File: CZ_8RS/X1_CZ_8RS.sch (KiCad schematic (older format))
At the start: 68 parts, among them IC1 74LS541, IC10 74LS04, IC11 74LS20, IC12 8251, IC13 74LS08, IC14 74LS01, IC15 MAX232, IC16 74LS74, IC17 74LS32, IC18 MAX232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

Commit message: Add files via upload
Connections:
- net at IC17.4: now also IC16.5 (Q); no longer IC16.6 (~Q)
- no-connect marks 23 -> 22
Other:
- moved on the sheet: IC12, IC14A, IC14C, IC14D, IC16A, IC16B, IC17B, IC17D, IC2B, IC2D, IC4A, IC4B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

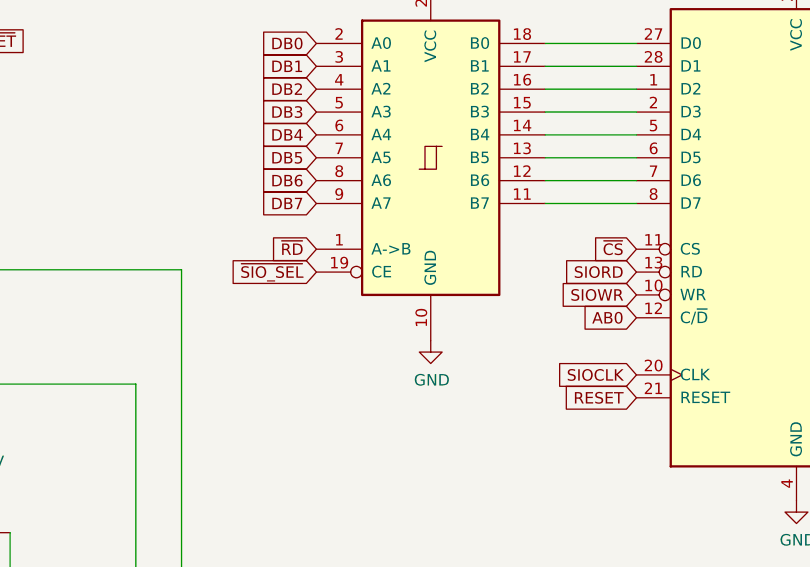
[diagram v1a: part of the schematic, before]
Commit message: corrected siosel, siord, and siowr line tag names
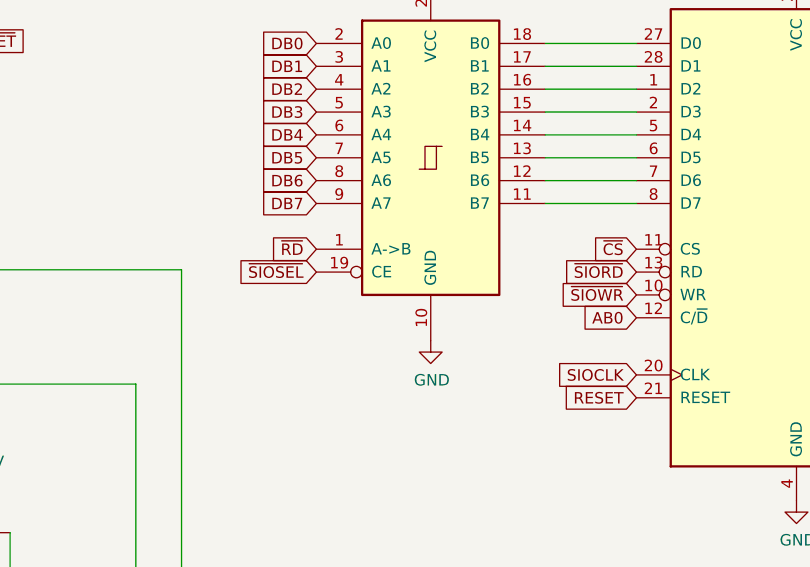
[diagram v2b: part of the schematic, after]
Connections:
- net SIORD is gone; now on net ~SIORD: IC12.13 (RD)
- net SIOWR is gone; now on net ~SIOWR: IC12.10 (WR)
- net ~SIO_SEL is gone; now on net ~SIOSEL: IC5.19 (CE)
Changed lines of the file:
@@
 ~RD
 Text GLabel 3840 5560 0    50   Input ~ 0
-~SIO_SEL
+~SIOSEL
 $Comp
 L power:+5V #PWR0134
@@
 ~CS
 Text GLabel 5240 5560 0    50   Input ~ 0
-SIORD
+~SIORD
 Text GLabel 5240 5660 0    50   Input ~ 0
-SIOWR
+~SIOWR
 Text GLabel 5240 5760 0    50   Input ~ 0
 AB0

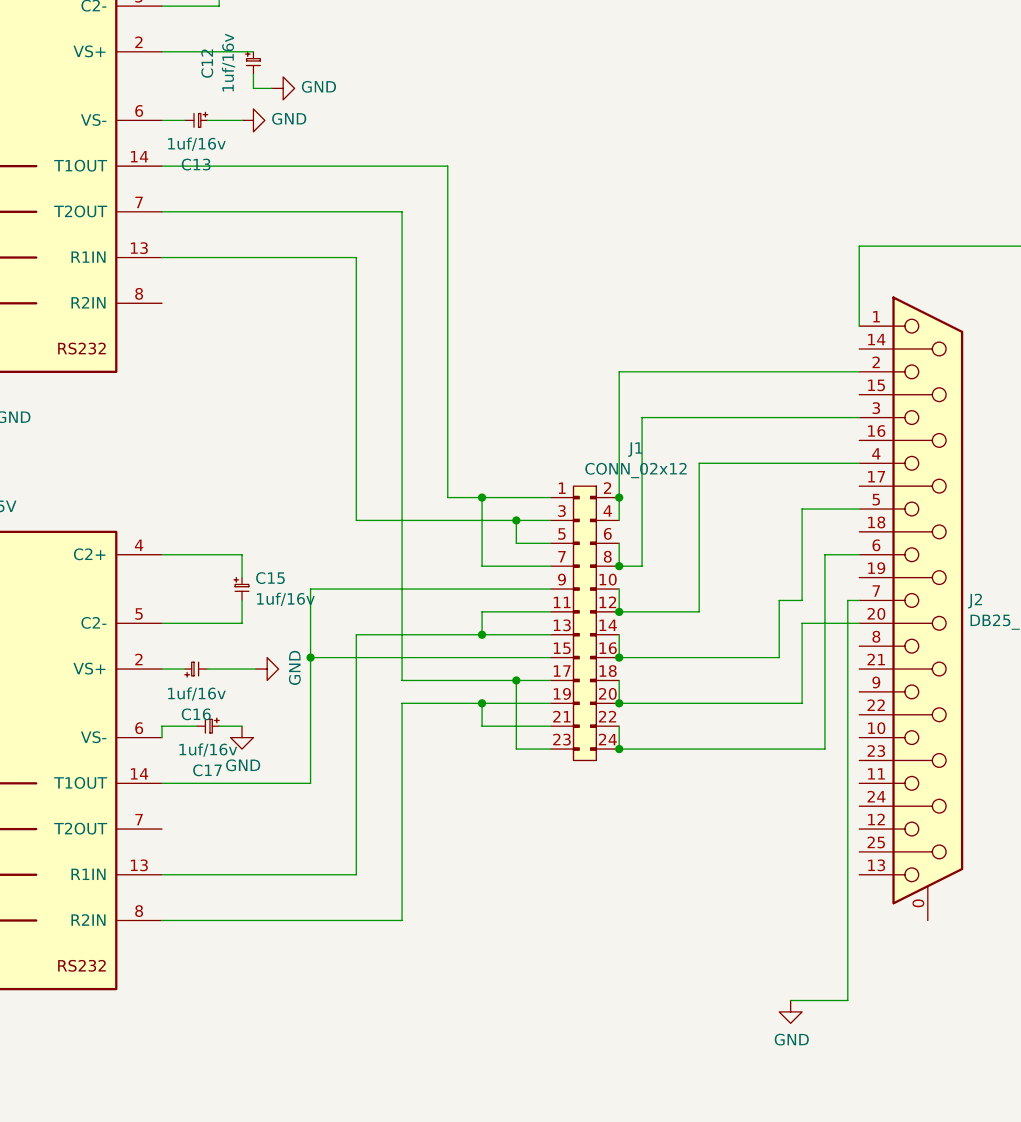
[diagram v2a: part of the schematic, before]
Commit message: added component names and jumper values
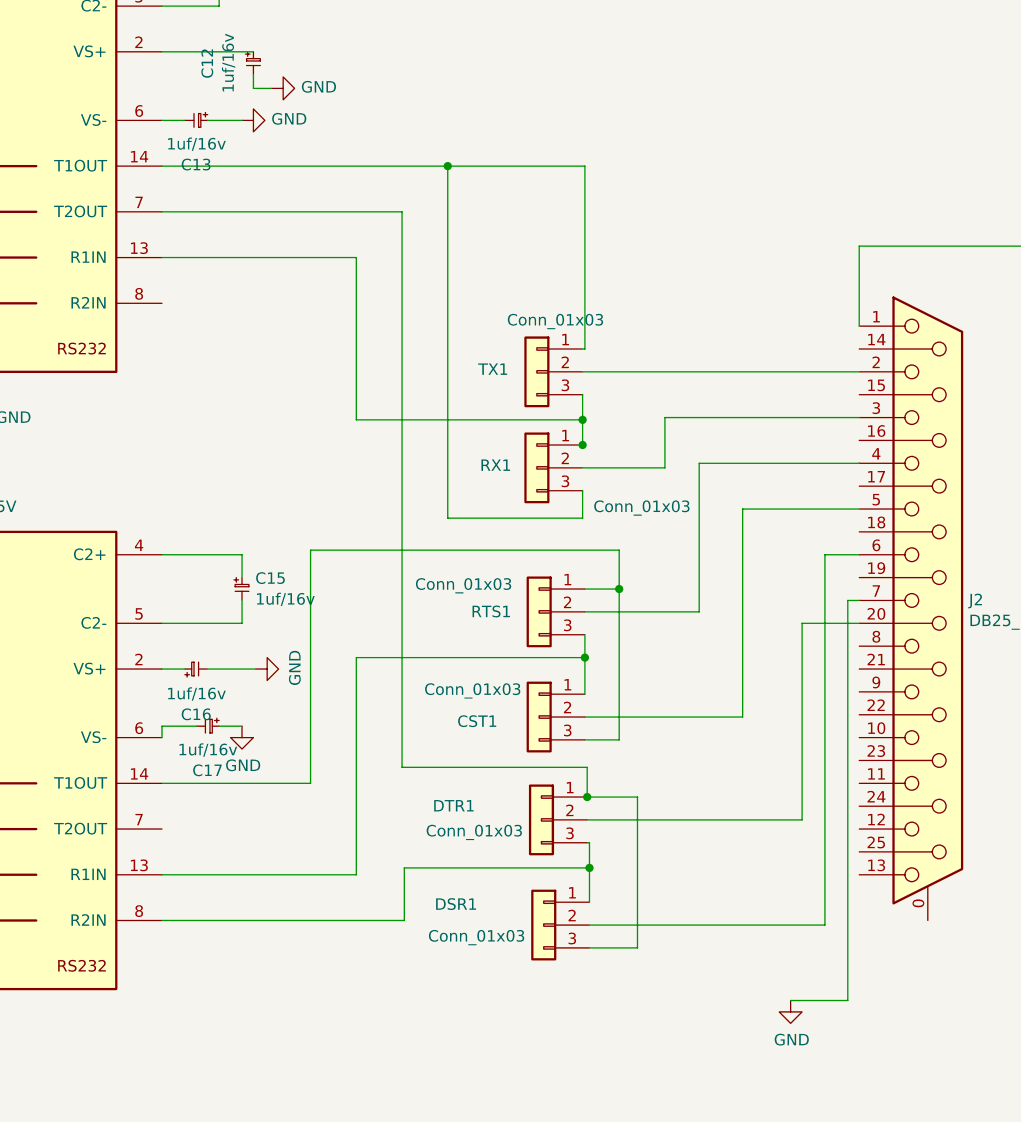
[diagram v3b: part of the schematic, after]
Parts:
- removed J1: CONN_02x12, Connector_PinHeader_2.54mm:PinHeader_2x12_P2.54mm_Vertical, symbol agg-kicad:CONN_02x12
- added CST1, DSR1, DTR1, RTS1, RX1, TX1: Conn_01x03, Connector_PinHeader_2.54mm:PinHeader_1x03_P2.54mm_Vertical, symbol Connector_Generic:Conn_01x03
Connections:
- net at IC15.14 (T1OUT): now also RX1.3 (Pin_3), TX1.1 (Pin_1)
- net at J2.4: now also RTS1.2 (Pin_2)
- net at IC18.13 (R1IN): now also CST1.1 (Pin_1), RTS1.3 (Pin_3)
- net at J2.5: now also CST1.2 (Pin_2)
- net at IC18.14 (T1OUT): now also CST1.3 (Pin_3), RTS1.1 (Pin_1)
- net at IC15.7 (T2OUT): now also DSR1.3 (Pin_3), DTR1.1 (Pin_1)
- net at J2.20 (P20): now also DTR1.2 (Pin_2)
- net at IC18.8 (R2IN): now also DSR1.1 (Pin_1), DTR1.3 (Pin_3)
- net at J2.2: now also TX1.2 (Pin_2)
- net at J2.6: now also DSR1.2 (Pin_2)
- net at IC15.13 (R1IN): now also RX1.1 (Pin_1), TX1.3 (Pin_3)
- net at J2.3: now also RX1.2 (Pin_2)
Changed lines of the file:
@@
 	15400 10350 16250 10350
-Wire Wire Line
-	18200 11450 18450 11450
 Wire Wire Line
 	18300 11650 18450 11650
@@
 Wire Wire Line
 	10350 14250 10250 14250
-$Comp
-L agg-kicad:CONN_02x12 J1
-U 1 1 645D5FD5
-P 17300 11400
-F 0 "J1" H 17475 11615 50  0000 C CNN
-F 1 "CONN_02x12" H 17475 11524 50  0000 C CNN
-F 2 "Connector_PinHeader_2.54mm:PinHeader_2x12_P2.54mm_Vertical" H 17300 11400 50  0001 C CNN
-F 3 "" H 17300 11400 50  0001 C CNN
-	1    17300 11400
-	1    0    0    -1
-$EndComp
-Wire Wire Line
-	17400 10850 17400 11400
-Wire Wire Line
-	17400 10850 18450 10850
-Wire Wire Line
-	17500 11050 18450 11050
 Wire Wire Line
 	18200 11950 18450 11950
@@
 Wire Wire Line
 	18400 13600 18150 13600
-Wire Wire Line
-	18200 11850 18100 11850
-Wire Wire Line
-	18200 11450 18200 11850
-Wire Wire Line
-	16650 11400 16800 11400
-Wire Wire Line
-	15400 13250 16450 13250
 $Comp
 L Device:C C58
@@
 	10300 13800 12250 13800
 Wire Wire Line
-	18300 12500 17400 12500
-Wire Wire Line
-	17400 12500 17400 12400
-Connection ~ 17400 12500
-Wire Wire Line
-	18300 11650 18300 12500
-Wire Wire Line
-	17400 12300 17400 12200
-Wire Wire Line
-	17400 12100 17400 12000
-Wire Wire Line
-	17400 11900 17400 11800
-Wire Wire Line
-	17400 11700 17400 11600
-Wire Wire Line
-	17400 12300 18200 12300
-Connection ~ 17400 12300
-Wire Wire Line
-	18200 11950 18200 12300
-Wire Wire Line
-	18100 12100 17400 12100
-Connection ~ 17400 12100
-Wire Wire Line
-	18100 11850 18100 12100
-Wire Wire Line
 	17750 11250 17750 11900
 Wire Wire Line
-	17750 11900 17400 11900
-Wire Wire Line
 	17750 11250 18450 11250
-Connection ~ 17400 11900
-Wire Wire Line
-	17500 11700 17400 11700
-Connection ~ 17400 11700
-Wire Wire Line
-	17500 11050 17500 11700
-Wire Wire Line
-	17400 11400 17400 11500
-Connection ~ 17400 11400
-Wire Wire Line
-	16650 9950 16650 11400
-Wire Wire Line
-	16450 12200 16950 12200
-Wire Wire Line
-	16450 10150 16450 12200
-Wire Wire Line
-	16050 11800 16050 12100
-Connection ~ 16050 12100
-Wire Wire Line
-	16050 11800 17100 11800
-Wire Wire Line
-	16050 12100 17100 12100
-Wire Wire Line
-	16050 12100 16050 12650
-Wire Wire Line
-	16250 12000 16800 12000
-Wire Wire Line
-	16450 12300 16450 13250
-Wire Wire Line
-	16450 12300 16800 12300
-Wire Wire Line
-	16250 12000 16250 13050
-Wire Wire Line
-	16800 12400 16800 12300
-Connection ~ 16800 12300
-Wire Wire Line
-	16800 11900 16800 12000
-Connection ~ 16800 12000
-Connection ~ 16800 11400
-Wire Wire Line
-	16800 11400 17100 11400
-Wire Wire Line
-	16250 10350 16250 11500
-Wire Wire Line
-	16250 11500 16950 11500
-Wire Wire Line
-	16800 11900 17100 11900
-Wire Wire Line
-	16800 12000 17100 12000
-Wire Wire Line
-	16800 12400 17100 12400
-Wire Wire Line
-	16800 12300 17100 12300
-Wire Wire Line
-	17100 12500 16950 12500
-Wire Wire Line
-	16950 12500 16950 12200
-Connection ~ 16950 12200
-Wire Wire Line
-	16950 12200 17100 12200
-Connection ~ 16950 11500
-Wire Wire Line
-	16950 11500 17100 11500
-Wire Wire Line
-	16950 11500 16950 11600
-Wire Wire Line
-	16950 11600 17100 11600
-Wire Wire Line
-	16800 11400 16800 11700
-Wire Wire Line
-	16800 11700 17100 11700
+Wire Wire Line
+	16250 10350 16250 11060
 Wire Wire Line
 	15600 9750 15750 9750
@@
 	3250 9700 3250 10100
 $Comp
-L power:GND #PWR?
+L power:GND #PWR0165
 U 1 1 6637E0F8
 P 15880 9610
-F 0 "#PWR?" H 15880 9360 50  0001 C CNN
+F 0 "#PWR0165" H 15880 9360 50  0001 C CNN
 F 1 "GND" V 15885 9482 50  0000 R CNN
 F 2 "" H 15880 9610 50  0001 C CNN
@@
 	15800 9610 15800 9550
 $Comp
-L power:GND #PWR?
+L power:GND #PWR0168
 U 1 1 663F6C4F
 P 15810 12150
-F 0 "#PWR?" H 15810 11900 50  0001 C CNN
+F 0 "#PWR0168" H 15810 11900 50  0001 C CNN
 F 1 "GND" H 15815 11977 50  0000 C CNN
 F 2 "" H 15810 12150 50  0001 C CNN
@@
 Wire Wire Line
 	9560 6200 9690 6200
+$Comp
+L Connector_Generic:Conn_01x03 TX1
+U 1 1 661F9765
+P 17040 10850
+F 0 "TX1" H 17230 10860 50  0000 C CNN
+F 1 "Conn_01x03" H 16958 11076 50  0000 C CNN
+F 2 "Connector_PinHeader_2.54mm:PinHeader_1x03_P2.54mm_Vertical" H 17040 10850 50  0001 C CNN
+F 3 "~" H 17040 10850 50  0001 C CNN
+	1    17040 10850
+	-1   0    0    -1
+$EndComp
+$Comp
+L Connector_Generic:Conn_01x03 RTS1
+U 1 1 661FD54E
+P 17050 11900
+F 0 "RTS1" H 17260 11900 50  0000 C CNN
+F 1 "Conn_01x03" H 17380 12020 50  0000 C CNN
+F 2 "Connector_PinHeader_2.54mm:PinHeader_1x03_P2.54mm_Vertical" H 17050 11900 50  0001 C CNN
+F 3 "~" H 17050 11900 50  0001 C CNN
+	1    17050 11900
+	-1   0    0    -1
+$EndComp
+$Comp
+L Connector_Generic:Conn_01x03 CST1
+U 1 1 662348C6
+P 17050 12360
+F 0 "CST1" H 17320 12340 50  0000 C CNN
+F 1 "Conn_01x03" H 17340 12480 50  0000 C CNN
+F 2 "Connector_PinHeader_2.54mm:PinHeader_1x03_P2.54mm_Vertical" H 17050 12360 50  0001 C CNN
+F 3 "~" H 17050 12360 50  0001 C CNN
+	1    17050 12360
+	-1   0    0    -1
+$EndComp
+$Comp
+L Connector_Generic:Conn_01x03 RX1
+U 1 1 6626BB42
+P 17040 11270
+F 0 "RX1" H 17220 11280 50  0000 C CNN
+F 1 "Conn_01x03" H 16580 11100 50  0000 C CNN
+F 2 "Connector_PinHeader_2.54mm:PinHeader_1x03_P2.54mm_Vertical" H 17040 11270 50  0001 C CNN
+F 3 "~" H 17040 11270 50  0001 C CNN
+	1    17040 11270
+	-1   0    0    -1
+$EndComp
+Wire Wire Line
+	17240 10850 18450 10850
+Wire Wire Line
+	17600 11270 17240 11270
+Wire Wire Line
+	17600 11270 17600 11050
+Wire Wire Line
+	17600 11050 18450 11050
+Wire Wire Line
+	16650 9950 17250 9950
+Wire Wire Line
+	17250 9950 17250 10750
+Wire Wire Line
+	17250 10750 17240 10750
+Connection ~ 16650 9950
+Wire Wire Line
+	17240 11370 17240 11490
+Wire Wire Line
+	17240 11490 16650 11490
+Wire Wire Line
+	16650 9950 16650 11490
+Wire Wire Line
+	16250 11060 17240 11060
+Wire Wire Line
+	17240 11060 17240 10950
+Wire Wire Line
+	17240 11060 17240 11170
+Wire Wire Line
+	17240 11170 17250 11170
+Connection ~ 17240 11060
+Connection ~ 17240 11170
+$Comp
+L Connector_Generic:Conn_01x03 DTR1
+U 1 1 6689A38C
+P 17060 12810
+F 0 "DTR1" H 17350 12870 50  0000 L CNN
+F 1 "Conn_01x03" H 17140 12761 50  0000 L CNN
+F 2 "Connector_PinHeader_2.54mm:PinHeader_1x03_P2.54mm_Vertical" H 17060 12810 50  0001 C CNN
+F 3 "~" H 17060 12810 50  0001 C CNN
+	1    17060 12810
+	-1   0    0    -1
+$EndComp
+$Comp
+L Connector_Generic:Conn_01x03 DSR1
+U 1 1 668CC284
+P 17070 13270
+F 0 "DSR1" H 17360 13360 50  0000 L CNN
+F 1 "Conn_01x03" H 17150 13221 50  0000 L CNN
+F 2 "Connector_PinHeader_2.54mm:PinHeader_1x03_P2.54mm_Vertical" H 17070 13270 50  0001 C CNN
+F 3 "~" H 17070 13270 50  0001 C CNN
+	1    17070 13270
+	-1   0    0    -1
+$EndComp
+Wire Wire Line
+	17250 11900 17750 11900
+Wire Wire Line
+	17250 11800 17400 11800
+Wire Wire Line
+	17400 11800 17400 11630
+Wire Wire Line
+	17400 11630 16050 11630
+Wire Wire Line
+	16050 11630 16050 12650
+Wire Wire Line
+	17250 12000 17250 12100
+Wire Wire Line
+	17250 12100 16250 12100
+Wire Wire Line
+	16250 12100 16250 13050
+Wire Wire Line
+	17250 12100 17250 12260
+Connection ~ 17250 12100
+Wire Wire Line
+	17250 12360 17940 12360
+Wire Wire Line
+	17940 12360 17940 11450
+Wire Wire Line
+	17940 11450 18450 11450
+Wire Wire Line
+	17400 11800 17400 12460
+Wire Wire Line
+	17400 12460 17250 12460
+Connection ~ 17400 11800
+Wire Wire Line
+	18200 12810 17260 12810
+Wire Wire Line
+	18200 11950 18200 12810
+Wire Wire Line
+	16450 12580 17260 12580
+Wire Wire Line
+	17260 12580 17260 12710
+Wire Wire Line
+	16450 10150 16450 12580
+Wire Wire Line
+	17260 12710 17480 12710
+Wire Wire Line
+	17480 12710 17480 13370
+Wire Wire Line
+	17480 13370 17270 13370
+Connection ~ 17260 12710
+Wire Wire Line
+	17270 13170 17270 13020
+Wire Wire Line
+	17270 12910 17260 12910
+Wire Wire Line
+	17270 13270 18300 13270
+Wire Wire Line
+	18300 11650 18300 13270
+Wire Wire Line
+	17270 13020 16460 13020
+Wire Wire Line
+	16460 13020 16460 13250
+Wire Wire Line
+	15400 13250 16460 13250
+Connection ~ 17270 13020
+Wire Wire Line
+	17270 13020 17270 12910
 $EndSCHEMATC
